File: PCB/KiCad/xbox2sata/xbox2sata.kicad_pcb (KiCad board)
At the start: 2 copper layers, 62.8 x 68.6 mm, 44 parts, among them IC1 TLV1117LV12DCYR, J1 61203921621, J2 67800-8025, J3 90151-2140, U1 88SA8052, Y1 ABLS-25.000MHZ-B4-F-T

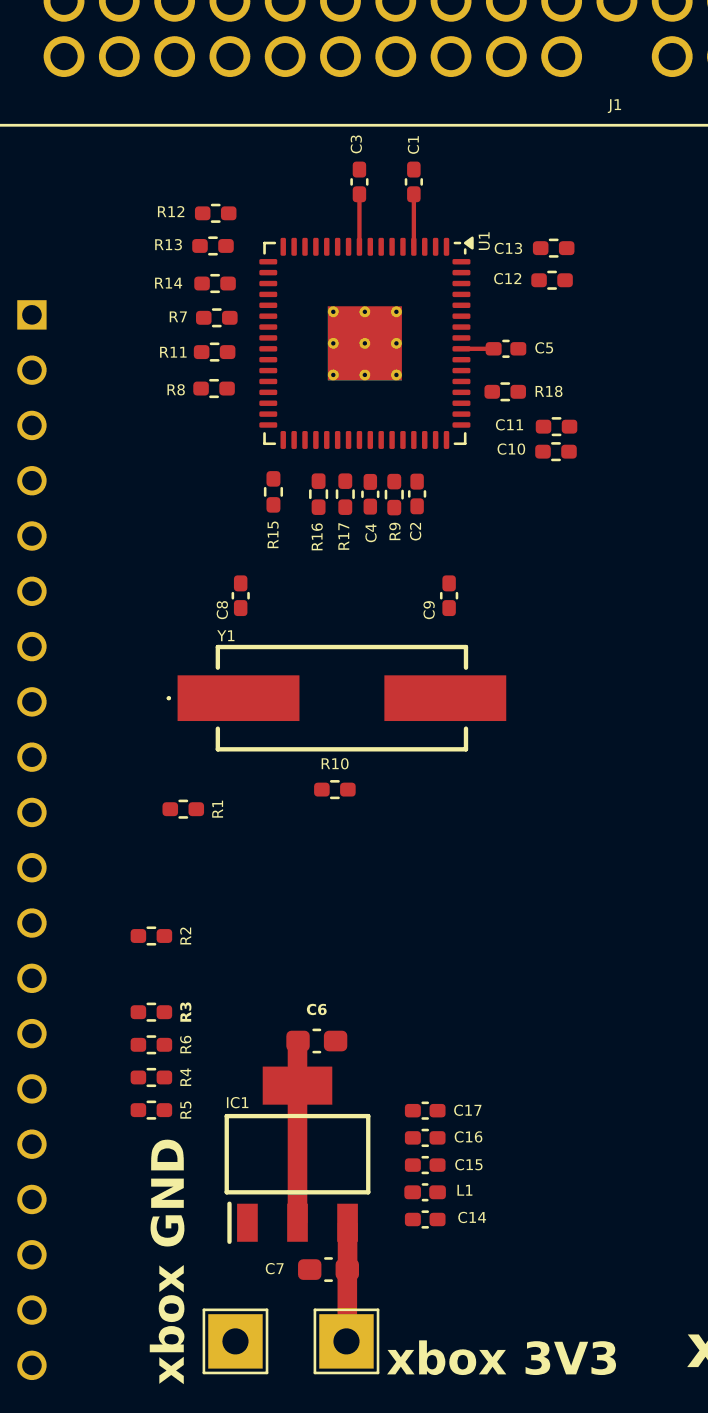
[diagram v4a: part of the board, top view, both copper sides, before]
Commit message: oscillator circuit corrected
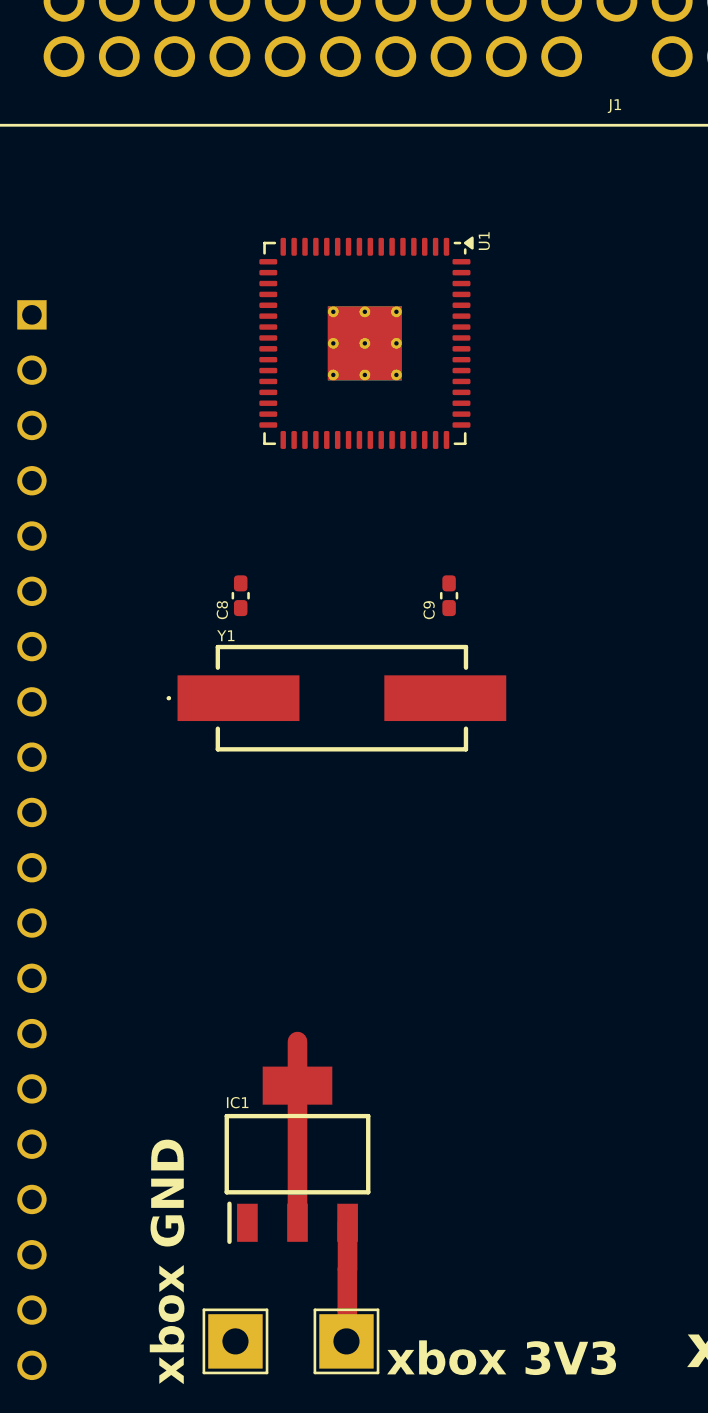
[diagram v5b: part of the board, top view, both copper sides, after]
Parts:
- removed C1, C15, C16, C2, C3, C4, C5: 100nF, Capacitor_SMD:C_0402_1005Metric_Pad0.74x0.62mm_HandSolder
- removed C10, C11, C12, C13: 10nF, Resistor_SMD:R_0402_1005Metric_Pad0.72x0.64mm_HandSolder
- removed C14, C17: 10nF, Capacitor_SMD:C_0402_1005Metric_Pad0.74x0.62mm_HandSolder
- removed C6, C7: 1uF, Capacitor_SMD:C_0603_1608Metric_Pad1.08x0.95mm_HandSolder
- removed L1: L, Inductor_SMD:L_0402_1005Metric_Pad0.77x0.64mm_HandSolder
- removed R1: 5.6K, Resistor_SMD:R_0402_1005Metric_Pad0.72x0.64mm_HandSolder
- removed R10: 1M, Resistor_SMD:R_0402_1005Metric_Pad0.72x0.64mm_HandSolder
- removed R11: 100, Resistor_SMD:R_0402_1005Metric_Pad0.72x0.64mm_HandSolder
- removed R12, R13, R14, R16, R17, R18, R3, R4, R5, R6, R7, R8, R9: 10K, Resistor_SMD:R_0402_1005Metric_Pad0.72x0.64mm_HandSolder
- removed R15, R2: 4.7K, Resistor_SMD:R_0402_1005Metric_Pad0.72x0.64mm_HandSolder
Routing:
- net 1V2: track 12.3 -> 8.36 mm
- net 3V3: track 7.88 -> 5.47 mm
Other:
- board text removed: "${REFERENCE}"

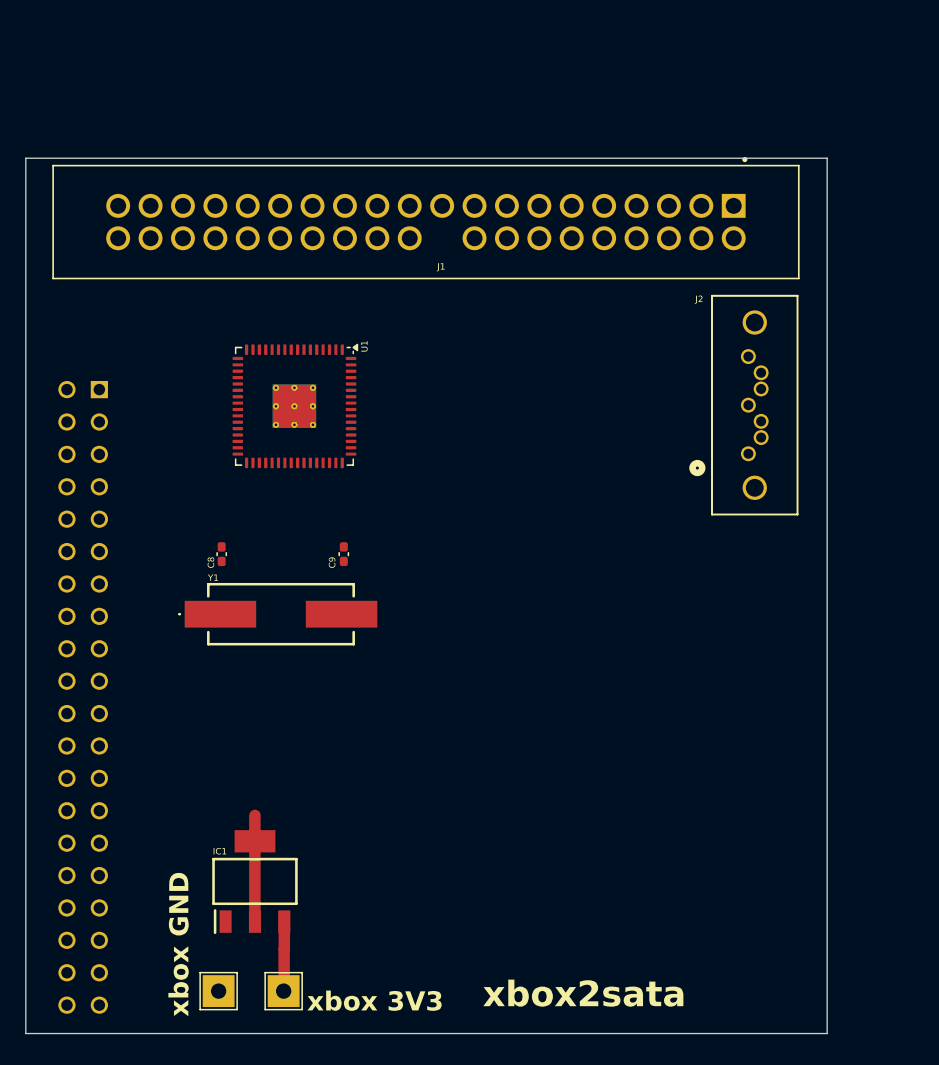
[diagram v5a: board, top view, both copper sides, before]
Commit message: bill of matierals
spreadsheet for bill of materials,
IDE female socket changed to cheaper option,
SATA socket changed to right angle, recommend by doofus.
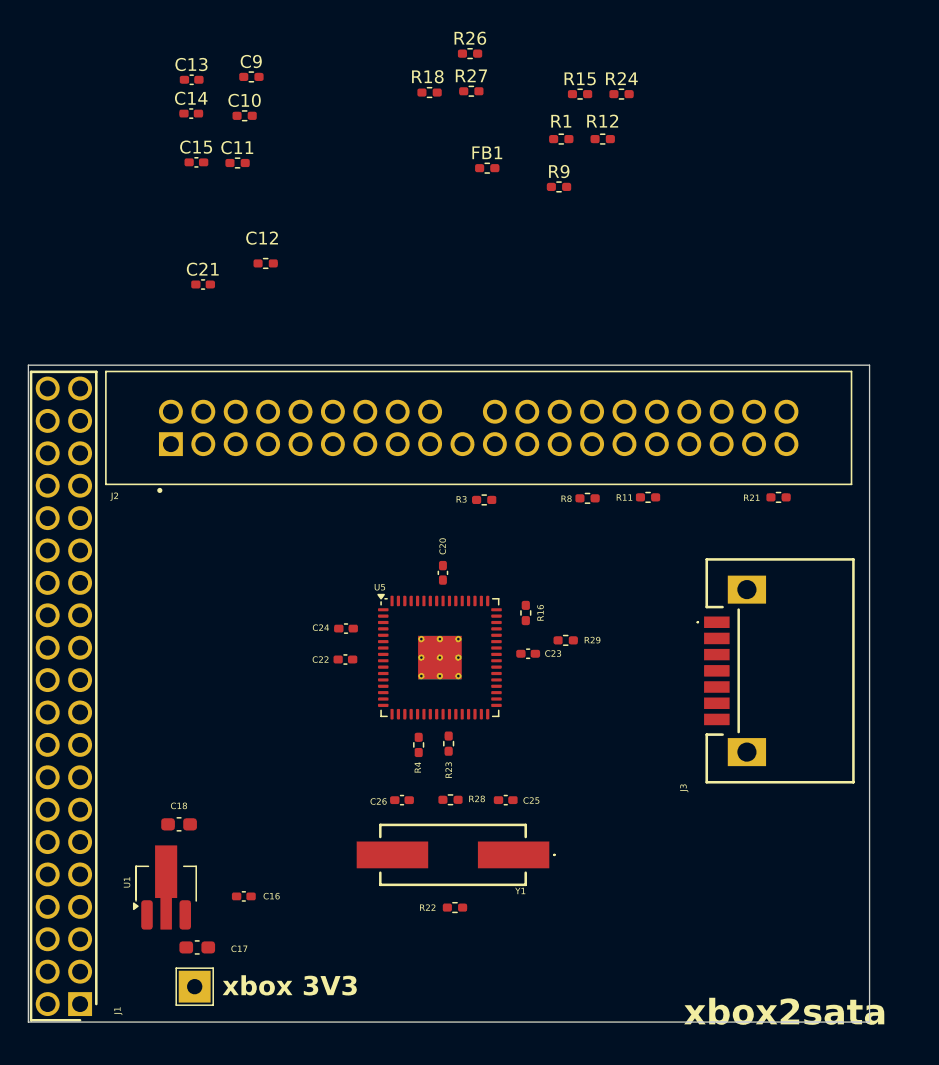
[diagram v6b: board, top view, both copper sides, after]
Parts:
- removed IC1: TLV1117LV12DCYR, xbox2sata:SOT230P700X180-4N
- removed the J2 at (160.6, 67.3)
- removed TP1: xbox_ground, TestPoint:TestPoint_THTPad_2.5x2.5mm_Drill1.2mm
- added C10: 10nF, Resistor_SMD:R_0402_1005Metric_Pad0.72x0.64mm_HandSolder, F.Cu at (121.1, 40.8)
- added C11: 10nF, Resistor_SMD:R_0402_1005Metric_Pad0.72x0.64mm_HandSolder, F.Cu at (120.5, 44.5)
- added C12: 10nF, Resistor_SMD:R_0402_1005Metric_Pad0.72x0.64mm_HandSolder, F.Cu at (122.7, 52.4)
- added C13: 100nF, Capacitor_SMD:C_0402_1005Metric_Pad0.74x0.62mm_HandSolder, F.Cu at (116.9, 38.0)
- added C14: 100nF, Capacitor_SMD:C_0402_1005Metric_Pad0.74x0.62mm_HandSolder, F.Cu at (116.9, 40.6)
- added C15: 10nF, Capacitor_SMD:C_0402_1005Metric_Pad0.74x0.62mm_HandSolder, F.Cu at (117.3, 44.5)
- added C16: 10nF, Capacitor_SMD:C_0402_1005Metric_Pad0.74x0.62mm_HandSolder, F.Cu at (121.0, 102.0)
- added C17: 10uf, Capacitor_SMD:C_0603_1608Metric_Pad1.08x0.95mm_HandSolder, F.Cu at (117.3, 106.0)
- added C18: 10uF, Capacitor_SMD:C_0603_1608Metric_Pad1.08x0.95mm_HandSolder, F.Cu at (115.9, 96.4)
- added C20: 100nF, Capacitor_SMD:C_0402_1005Metric_Pad0.74x0.62mm_HandSolder, F.Cu at (136.6, 76.7)
- added C21: 100nF, Capacitor_SMD:C_0402_1005Metric_Pad0.74x0.62mm_HandSolder, F.Cu at (117.8, 54.0)
- added C22: 100nF, Capacitor_SMD:C_0402_1005Metric_Pad0.74x0.62mm_HandSolder, F.Cu at (129.0, 83.5)
- added C23: 100nF, Capacitor_SMD:C_0402_1005Metric_Pad0.74x0.62mm_HandSolder, F.Cu at (143.3, 83.0)
- added C24: 100nF, Capacitor_SMD:C_0402_1005Metric_Pad0.74x0.62mm_HandSolder, F.Cu at (129.0, 81.0)
- added C9: 10nF, Resistor_SMD:R_0402_1005Metric_Pad0.72x0.64mm_HandSolder, F.Cu at (121.6, 37.8)
- added FB1: 60R, Resistor_SMD:R_0402_1005Metric_Pad0.72x0.64mm_HandSolder, F.Cu at (140.1, 44.9)
- added J1: 929975-01-20-RK, xbox2sata:RHDR40W76P254_2X20_5080X508X826P, F.Cu at (107.1, 87.6)
- added R1: 4.7K, Resistor_SMD:R_0402_1005Metric_Pad0.72x0.64mm_HandSolder, F.Cu at (145.9, 42.6)
- added R11: 10K, Resistor_SMD:R_0402_1005Metric_Pad0.72x0.64mm_HandSolder, F.Cu at (152.7, 70.7)
- added R12: 10K, Resistor_SMD:R_0402_1005Metric_Pad0.72x0.64mm_HandSolder, F.Cu at (149.1, 42.6)
- added R15: 10K, Resistor_SMD:R_0402_1005Metric_Pad0.72x0.64mm_HandSolder, F.Cu at (147.4, 39.1)
- added R16: 100K, Resistor_SMD:R_0402_1005Metric_Pad0.72x0.64mm_HandSolder, F.Cu at (143.1, 79.8)
- added R18: 10K, Resistor_SMD:R_0402_1005Metric_Pad0.72x0.64mm_HandSolder, F.Cu at (135.6, 39.0)
- added R21: 10K, Resistor_SMD:R_0402_1005Metric_Pad0.72x0.64mm_HandSolder, F.Cu at (162.9, 70.7)
- added R22: 1M, Resistor_SMD:R_0402_1005Metric_Pad0.72x0.64mm_HandSolder, F.Cu at (137.5, 102.9)
- added R23: 6.04K, Resistor_SMD:R_0402_1005Metric_Pad0.72x0.64mm_HandSolder, F.Cu at (137.1, 90.0)
- added R24: 10K, Resistor_SMD:R_0402_1005Metric_Pad0.72x0.64mm_HandSolder, F.Cu at (150.6, 39.1)
- added R26: 10K, Resistor_SMD:R_0402_1005Metric_Pad0.72x0.64mm_HandSolder, F.Cu at (138.7, 36.0)
- added R27: 4.7K, Resistor_SMD:R_0402_1005Metric_Pad0.72x0.64mm_HandSolder, F.Cu at (138.8, 38.9)
- added R28: 100, Resistor_SMD:R_0402_1005Metric_Pad0.72x0.64mm_HandSolder, F.Cu at (137.2, 94.5)
- added R29: 10K, Resistor_SMD:R_0402_1005Metric_Pad0.72x0.64mm_HandSolder, F.Cu at (146.2, 82.0)
- added R3: 5.6K, Resistor_SMD:R_0402_1005Metric_Pad0.72x0.64mm_HandSolder, F.Cu at (139.8, 70.9)
- added R4: 10K, Resistor_SMD:R_0402_1005Metric_Pad0.72x0.64mm_HandSolder, F.Cu at (134.7, 90.1)
- added R8: 4.7K, Resistor_SMD:R_0402_1005Metric_Pad0.72x0.64mm_HandSolder, F.Cu at (147.9, 70.8)
- added R9: 10K, Resistor_SMD:R_0402_1005Metric_Pad0.72x0.64mm_HandSolder, F.Cu at (145.7, 46.4)
- added U1: 1V2 voltage regulator, Package_TO_SOT_SMD:SOT-89-3_Handsoldering, F.Cu at (114.9, 101.0)
- J3: value 90151-2140 -> SATA-A-PL-SMT-K; footprint xbox2sata:RHDR40W70P254_2X20_5065X498X870P -> xbox2sata:SATAAPLSMTK; moved to F.Cu
- Y1: value ABLS-25.000MHZ-B4-F-T -> 25MHz
- moved J3 57.7 mm to (163.0, 84.3)
- moved C25 29.5 mm to (141.5, 94.5), turned to 180 degrees
- moved Y1 23.2 mm to (137.4, 98.8), turned to 180 degrees
- moved U5 22.8 mm to (136.4, 83.3), turned to 0 degrees
- moved C26 19.8 mm to (133.4, 94.5), turned to 0 degrees
- moved J2 16.7 mm to (139.4, 65.3), turned to 0 degrees
- moved TP2 6.98 mm to (117.1, 109.1)
- renumbered C8 to C25, C9 to C26, J1 to J2, U1 to U5
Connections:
- C25 pad 2: GND -> VSS
- C26 pad 2: GND -> VSS
- J2 pad 32: Net-(J1-Pad32) -> GND
- J2 pad 39: Net-(J1-Pad39) -> DASP-
- J3 pad 1: RESET- -> GND
- U5 pad 33: T0 -> GND
- U5 pad 34: PDIAG -> DASP-
- U5 pad 35: T1 -> T2
- U5 pad 65: unconnected-(U1-GND-Pad65) -> GND
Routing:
- net 1V2: track 8.36 -> 0.00 mm
- net 3V3: track 5.47 -> 0.05 mm
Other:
- board size 62.8 x 68.6 mm -> 66 x 51.5 mm
- board text removed: "xbox GND"

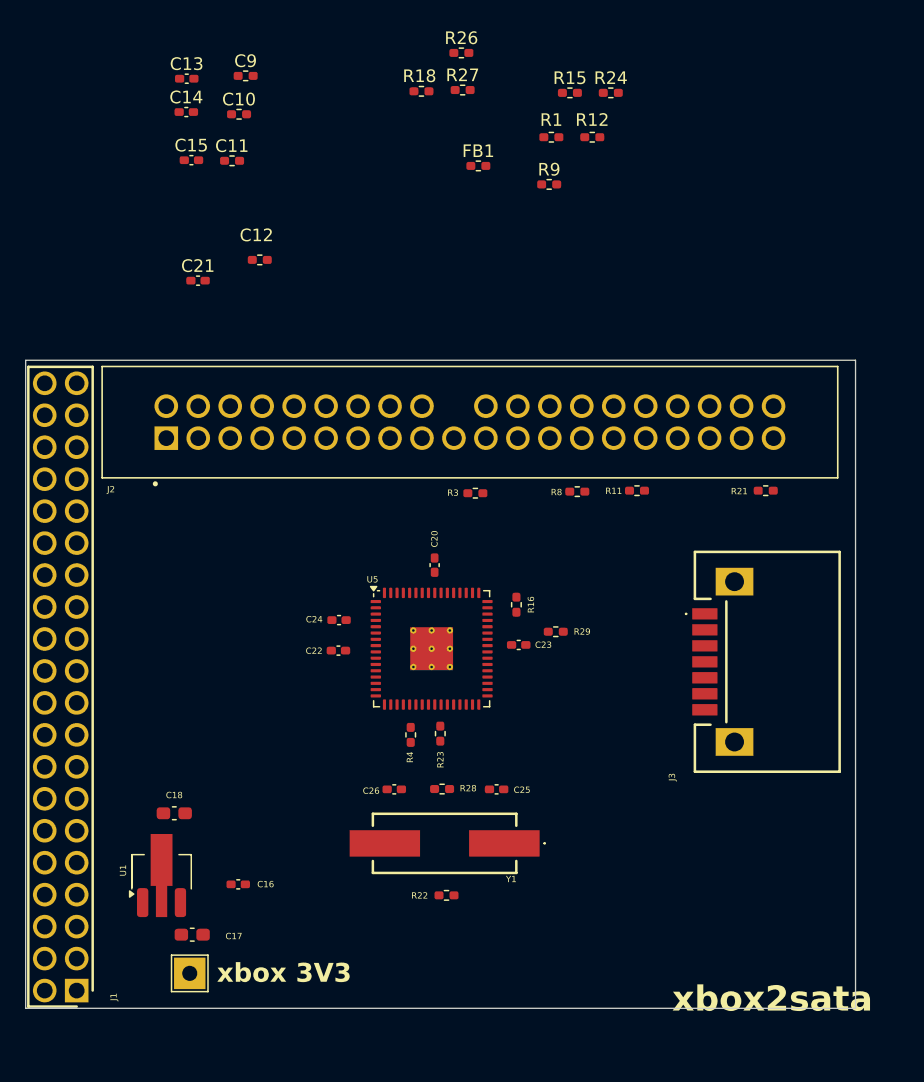
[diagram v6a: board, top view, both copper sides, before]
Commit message: reset and csel correct circuit from startech
10K resistor (R14) pull-up to 3V3 added to CSEL IDE pin 28
4.7K resistor (R19) pull-down to ground on T0 U5 pin 33 to device as IDE master
positive power supply icons changed from Global labels to power symbols
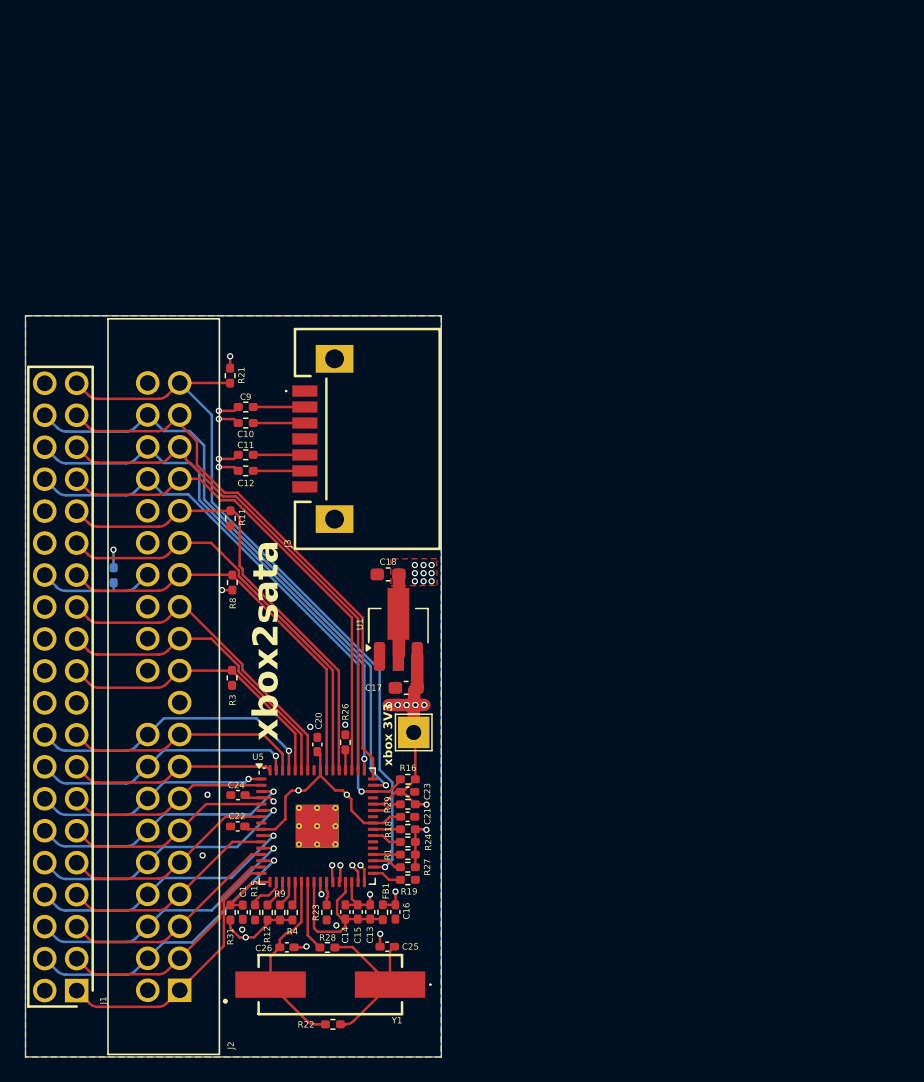
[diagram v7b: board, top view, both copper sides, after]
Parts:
- added C1: 4.7uF, Capacitor_SMD:C_0402_1005Metric_Pad0.74x0.62mm_HandSolder, F.Cu at (121.3, 104.2)
- added R14: 10K, Resistor_SMD:R_0402_1005Metric_Pad0.72x0.64mm_HandSolder, B.Cu at (111.1, 77.5)
- added R19: 4.7K, Resistor_SMD:R_0402_1005Metric_Pad0.72x0.64mm_HandSolder, F.Cu at (134.5, 101.7)
- added R31: 5.6K, Resistor_SMD:R_0402_1005Metric_Pad0.72x0.64mm_HandSolder, F.Cu at (120.4, 104.3)
- TP2: value xbox_3V3 -> from xbox 3V3
- moved R15 69.8 mm to (122.3, 104.3), turned to -90 degrees
- moved C13 67.8 mm to (131.5, 104.2), turned to 90 degrees
- moved R12 66.8 mm to (123.3, 104.3), turned to -90 degrees
- moved C14 64.8 mm to (129.5, 104.2), turned to 90 degrees
- moved R27 61.9 mm to (134.5, 100.7)
- moved R9 61.7 mm to (124.3, 104.3), turned to -90 degrees
- moved R24 61.7 mm to (134.5, 98.7), turned to 180 degrees
- moved C15 61.2 mm to (130.5, 104.2), turned to 90 degrees
- moved FB1 59.8 mm to (132.5, 104.2), turned to -90 degrees
- moved R18 58.7 mm to (134.5, 97.7), turned to 180 degrees
- moved R1 58.1 mm to (134.5, 99.7)
- moved R26 55.6 mm to (129.5, 90.7), turned to -90 degrees
- moved C21 45.7 mm to (134.4, 96.7)
- moved R21 43.5 mm to (120.3, 61.6), turned to -90 degrees
- moved J3 36.4 mm to (131.2, 66.6)
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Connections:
- C10 pad 1: RX_M -> TX_N
- C11 pad 1: TX_M -> RX_N
- C12 pad 2: Net-(J3-GND_3) -> Net-(J3-B+)
- C16 pad 1: 3V3 -> +3V3
- C17 pad 2: 3V3 -> +3V3
- C18 pad 1: 1V2 -> +1V2
- C20 pad 1: 1V2 -> +1V2
- C21 pad 1: 1V2 -> +1V2
- C22 pad 1: 1V2 -> GND
- C22 pad 2: GND -> +1V2
- C23 pad 1: 3V3 -> +3V3
- C24 pad 1: 3V3 -> GND
- C24 pad 2: GND -> +3V3
- FB1 pad 1: 3V3 -> +3V3
- J1 pad 20: unconnected-(J1-Pad20) -> GND
- J1 pad 29: unconnected-(J1-Pad29) -> DMACK-
- J3 pad S6: GND -> Net-(J3-B+)
- J3 pad S7: Net-(J3-GND_3) -> GND
- R1 pad 2: 3V3 -> +3V3
- R12 pad 2: 3V3 -> +3V3
- R16 pad 2: 3V3 -> +3V3
- R18 pad 1: 3V3 -> +3V3
- R21 pad 1: 3V3 -> +3V3
- R24 pad 1: 3V3 -> +3V3
- R27 pad 2: 3V3 -> +3V3
- R29 pad 2: 3V3 -> +3V3
- R4 pad 1: 3V3 -> +3V3
- R8 pad 1: 3V3 -> +3V3
- R9 pad 2: 3V3 -> +3V3
- TP2 pad 1: 3V3 -> +3V3
- U1 pad 2: 1V2 -> +1V2
- U1 pad 3: 3V3 -> +3V3
- U5 pad 17: RST- -> Net-(U5-RST_N)
- U5 pad 28: RX_M -> RX_N
- U5 pad 31: TX_M -> TX_N
- U5 pad 33: GND -> Net-(U5-T0)
- U5 pad 38: T5 -> GND
- U5 pad 4: 3V3 -> +3V3
- U5 pad 41: 1V2 -> +1V2
- U5 pad 44: 3V3 -> +3V3
- U5 pad 56: 1V2 -> +1V2
- U5 pad 9: 1V2 -> +1V2
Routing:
- net DASP-: track 0.00 -> 59.8 mm, vias 0 -> 1
- net TX_P: track 0.00 -> 53.3 mm, vias 0 -> 2
- net TX_N: track 0.00 -> 50.7 mm, vias 0 -> 2
- net RX_N: track 0.00 -> 50.4 mm, vias 0 -> 2
- net RX_P: track 0.00 -> 50.3 mm, vias 0 -> 2
- net CS1-: track 0.00 -> 48.7 mm, vias 0 -> 1
- net PDIAG-: track 0.00 -> 45.6 mm, vias 0 -> 1
- net CS0-: track 0.00 -> 44.3 mm
- net DA2: track 0.00 -> 43.2 mm, vias 0 -> 1
- net DA0: track 0.00 -> 41.1 mm
- net DA1: track 0.00 -> 39.5 mm
- net INTRQ: track 0.00 -> 37.5 mm
- net +3V3: track 0.00 -> 37.1 mm, vias 0 -> 13
- net DMACK-: track 0.00 -> 33.7 mm
- net IORDY: track 0.00 -> 31.9 mm
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- added copper zone on F.Cu, net +1V2
- added copper zone on In2.Cu, net +1V2
- added copper zone on In1.Cu, net +3V3
- added copper zone on B.Cu, net GND
- added copper zone on F.Cu, net GND
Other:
- board size 66 x 51.5 mm -> 33 x 58.9 mm
- copper layers 2 -> 4
